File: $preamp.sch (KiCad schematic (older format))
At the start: 102 parts, among them P1 GND_RCA, P10 Jack_L, P11 Jack_R, P12 RCA2_L, P13 GND, P14 GND, P16 +15, P17 GND, P18 L_pow+, P19 R_pow+, P2 Instrum_R, P20 L_pentode, P21 R_pentode, P22 L_pentode_in, P23 R_pentode_in, P27 R_pow-, P28 L_pow-, P29 Gain_R_M, P3 GND_instrum, P30 Gain_R_L, P31 Gain_R_H, P32 Gain_L_M, P33 Gain_L_L, P34 Gain_L_H, P35 LED_Ca, P36 SW_1, P37 SW_com, P38 SW_2, P39 LED_An, P4 RCA1_R, P40 vol_R_H, P41 vol_L_L, P42 vol_L_H, P43 vol_R_M, P44 vol_R_L, P45 vol_L_M, P5 Instrum_L, P6 GND_RCA2, P7 RCA2_R, P8 RCA1_L, P9 GND_Jack1, U1 LM193, U2 TL074, U3 TL074, U5 TLE2426, U6 LM7812, U7 DG419, U8 DG419

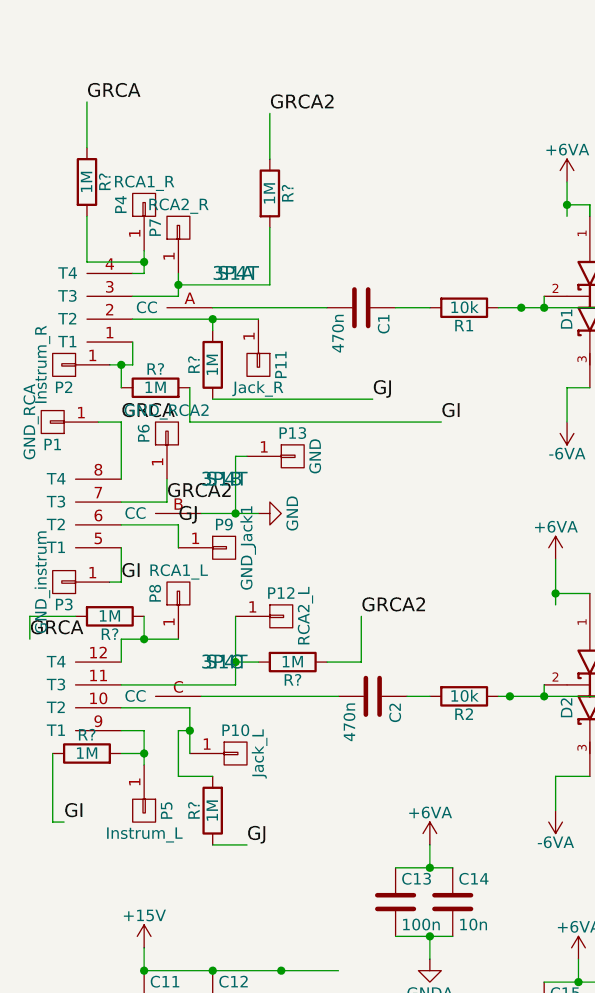
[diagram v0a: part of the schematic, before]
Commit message: 1M to gnd on all inputs
Added 1M to ground to avoid floating inputs
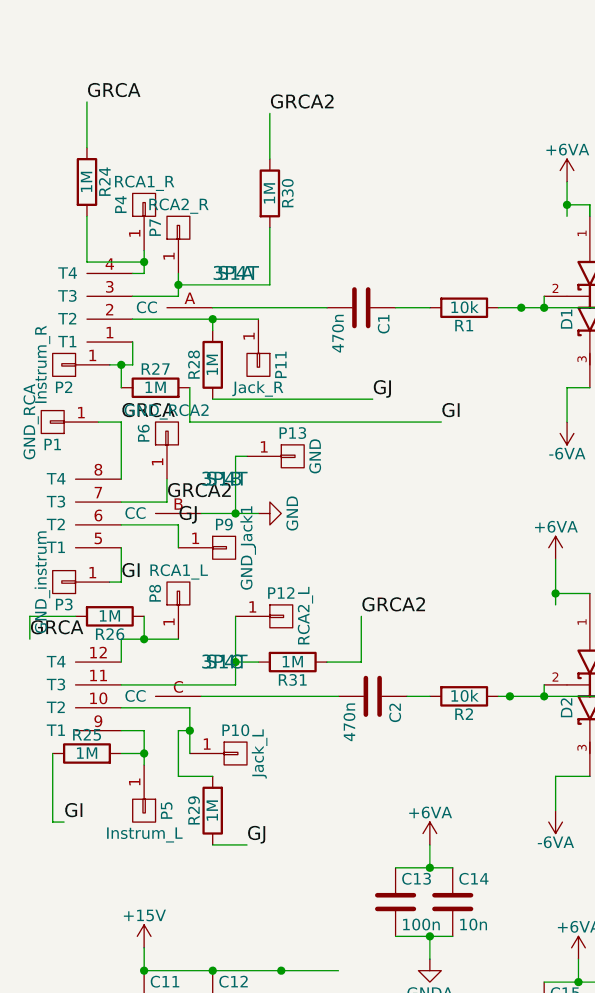
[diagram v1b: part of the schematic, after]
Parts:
- gave numbers to parts that had none: 8
